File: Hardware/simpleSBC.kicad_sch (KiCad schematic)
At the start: 65 parts, among them J1 Conn_02x07_Odd_Even, J5 USB_A, J6 USB_A, J7 RJ45_Wuerth_7499010121A, J9 Conn_01x06, SW1 SW_Push, U1 STM32MP157FAD1, U2 STMPS2252MTR, U5 USBLC6-4SC6, U6 LAN8742A, X1 ASCO, Y1 32.786, Y2 X53T-C20SSA-25.000MHz

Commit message: First Pass Routing
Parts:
- removed Y2: X53T-C20SSA-25.000MHz, symbol Device:Crystal
- added JP6, JP7: SolderJumper_3_Bridged12, Jumper:SolderJumper-3_P1.3mm_Bridged2Bar12_Pad1.0x1.5mm, symbol Jumper:SolderJumper_3_Bridged12
- added Y3: 24M, SimpleSBC:Crystal_2.00x1.60mm, symbol Device:Crystal_GND24
- JP1, JP2, JP3: footprint (none) -> Resistor_SMD:R_0402_1005Metric; now in the parts list
- SW1: footprint (none) -> Button_Switch_SMD:SW_SPST_Omron_B3FS-101xP
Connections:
- net GND: now also Y3.2, Y3.4
- net IO1: now also U1.1J1 (PA4)
- net IO5: no longer U1.W7 (PF7)
- net IO6: no longer U1.W8 (PG9)
- net PRT1: now also U1.W7 (PF7)
- net PRT2: now also U1.W8 (PG9)
- net USB_~{OC1}: now also U1.V9 (PF9)
- net USB_~{OC2}: now also U1.V7 (PE7)
- net at J5.1 (VBUS): now also JP7.2 (C); no longer U2.6 (OUT2)
- net USB2_D-: now reaches J5.2 (D-), U1.W10 (USB_DM2)
- net USB2_D+: now reaches J5.3 (D+), U1.V10 (USB_DP2)
- net at J6.1 (VBUS): now also JP6.2 (C); no longer U2.7 (OUT1)
- net USB1_D+: now reaches J6.2 (D-), U1.V14 (USB_DP1)
- net USB1_D-: now reaches J6.3 (D+), U1.W14 (USB_DM1)
- net at C44.1, U6.4 (XTAL2): now also Y3.1
- net at C42.1, U6.5 (XTAL1/CLKIN): now also Y3.3
- net +5V renamed VBUS
- new net PMIC_SWOUT: JP6.3 (B)
- new net VBUS1: U2.7 (OUT1)
- new net VBUS2: JP6.1 (A), U2.6 (OUT2)
- no-connect marks 78 -> 75
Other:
- sheet Power ports: added PMIC_SWOUT, PMIC_VBUSOTG; removed none
- note added: "TODO: - ADD PMIC BOOST with disconnect - DAC and ADC pins - Missing Pin Connections - What to do with OTG_VBUS (V16) - Disconnect DSI pins? - Check BOOT pin values - Last checkbox pg. 21 - DRAM LDM Question - OTG VBUS? - RJ45 LEDs?"
- note removed: "TODO: - Missing Pin Connections - What to do with OTG_VBUS (V16) - Disconnect DSI pins? - Check BOOT pin values - Last checkbox pg. 21 - DRAM LDM Question - OTG VBUS? - RJ45 LEDs?"
- moved on the sheet: C42, J5, J9, JP1, R62

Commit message: ERC/DRC Clean
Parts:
- removed J9: Conn_01x06, Connector_PinHeader_2.54mm:PinHeader_1x06_P2.54mm_Vertical, symbol Connector_Generic:Conn_01x06
- added J3, J9: Conn_02x10_Odd_Even, Connector_PinHeader_2.54mm:PinHeader_2x10_P2.54mm_Vertical, symbol Connector_Generic:Conn_02x10_Odd_Even
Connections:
- net +3V3: now also J3.20 (Pin_20), J9.20 (Pin_20)
- net GND: now also J3.19 (Pin_19), J9.19 (Pin_19)
- net PMIC_VBUSOTG: now also JP7.3 (B)
- net VBUS1: now also JP7.1 (A)
- net PD15: now reaches U1.1C2 (PD15)
- net PD15: now also J9.6 (Pin_6)
- net PD1: now reaches U1.A2 (PD1)
- net PD1: now also J9.12 (Pin_12)
- net PC6: now reaches U1.A4 (PC6)
- net PC6: now also J9.13 (Pin_13)
- net PD3: now reaches U1.A7 (PD3)
- net PD3: now also J9.16 (Pin_16)
- net PG15: now reaches U1.B1 (PG15)
- net PG15: now also J9.11 (Pin_11)
- net PE6: now reaches U1.B2 (PE6)
- net PE6: now also J3.16 (Pin_16)
- net PD7: now reaches U1.B3 (PD7)
- net PD7: now also J3.17 (Pin_17)
- net PA15: now reaches U1.B4 (PA15)
- net PA15: now also J9.1 (Pin_1)
- net PG6: now reaches U1.B5 (PG6)
- net PG6: now also J9.18 (Pin_18)
- net PB4: now reaches U1.B6 (PB4)
- net PB4: now also J9.15 (Pin_15)
- net PE5: now reaches U1.B7 (PE5)
- net PE5: now also J9.17 (Pin_17)
- net PA8: now reaches U1.B8 (PA8)
- net PA8: now also J3.15 (Pin_15)
- net PE12: now reaches U1.C1 (PE12)
- net PE12: now also J9.10 (Pin_10)
- net PC7: now reaches U1.C10 (PC7)
- net PC7: now also J9.2 (Pin_2)
- net PE0: now reaches U1.C2 (PE0)
- net PE0: now also J9.9 (Pin_9)
- net PD4: now reaches U1.C3 (PD4)
- net PD4: now also J9.8 (Pin_8)
- net PD5: now reaches U1.C4 (PD5)
- net PD5: now also J3.18 (Pin_18)
- net PD0: now reaches U1.C5 (PD0)
- net PD0: now also J9.14 (Pin_14)
- net PA9: now reaches U1.C6 (PA9)
- net PA9: now also J3.2 (Pin_2)
- net PB15: now reaches U1.C8 (PB15)
- net PB15: now also J3.14 (Pin_14)
- net PB9: now reaches U1.C9 (PB9)
- net PB9: now also J3.1 (Pin_1)
- net PG12: now reaches U1.D1 (PG12)
- net PG12: now also J3.13 (Pin_13)
- net PE15: now reaches U1.D3 (PE15)
- net PE15: now also J9.7 (Pin_7)
- net PD8: now reaches U1.E1 (PD8)
- net PD8: now also J3.12 (Pin_12)
- net PE13: now reaches U1.E3 (PE13)
- net PE13: now also J3.11 (Pin_11)
- net PE2: now reaches U1.P1 (PE2)
- net PE2: now also J9.3 (Pin_3)
- net PC2: now reaches U1.P2 (PC2)
- net PC2: now also J9.4 (Pin_4)
- net PB1: now reaches U1.U1 (PB1)
- net PB1: now also J3.7 (Pin_7)
- net PB0: now reaches U1.U2 (PB0)
- net PB0: now also J3.10 (Pin_10)
- net PC0: now reaches U1.U4 (PC0)
- net PC0: now also J3.4 (Pin_4)
- net PG10: now reaches U1.U7 (PG10)
- net PG10: now also J9.5 (Pin_5)
- net PD11: now reaches U1.U8 (PD11)
- net PD11: now also J3.3 (Pin_3)
- net PB12: now reaches U1.V3 (PB12)
- net PB12: now also J3.9 (Pin_9)
- net PB8: now reaches U1.V4 (PB8)
- net PB8: now also J3.8 (Pin_8)
- net IO1: no longer names the net of U1.1J1 (PA4)
- net IO3 renamed PA6
- net PA6: now also J3.6 (Pin_6)
- net IO4 renamed PF11
- net PF11: now also J3.5 (Pin_5)
- no-connect marks 75 -> 42
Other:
- moved on the sheet: JP7, R60

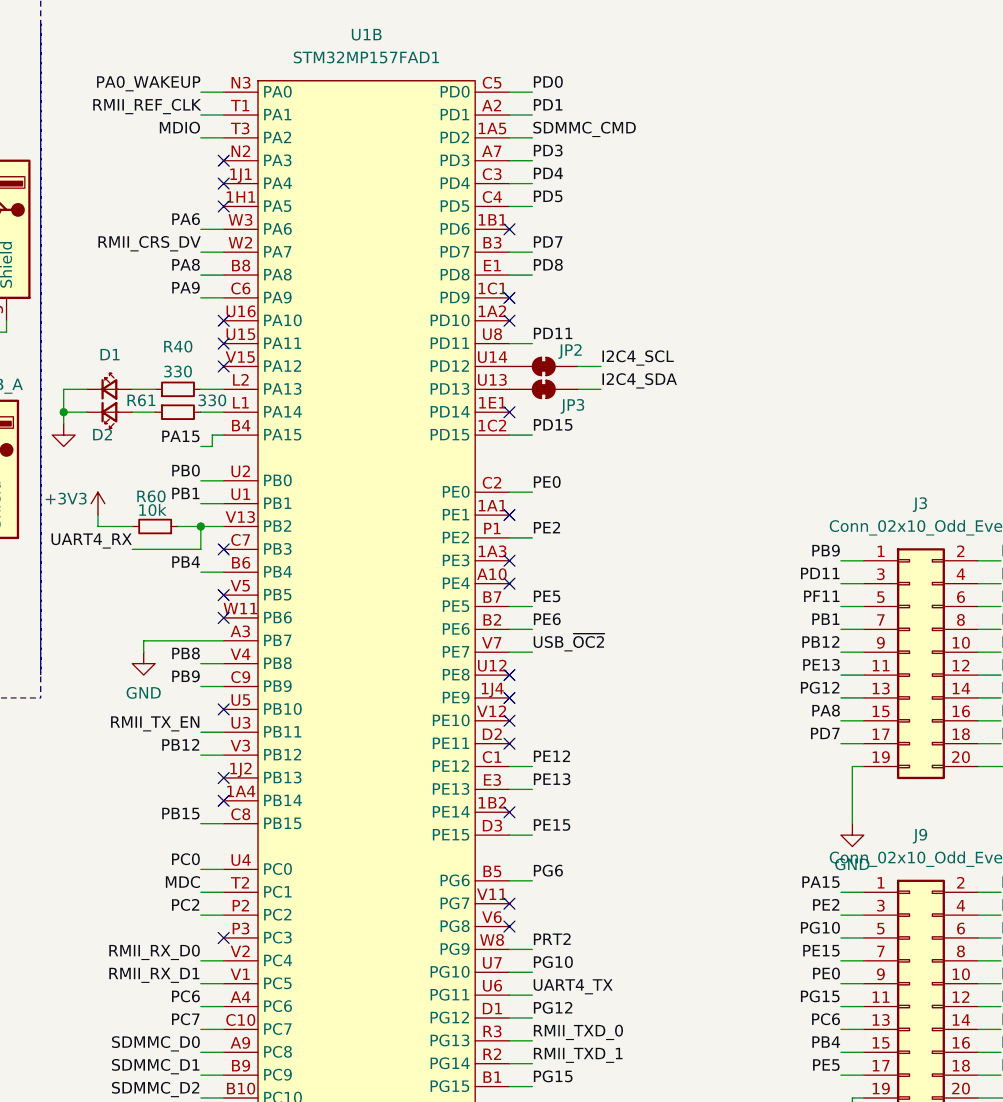
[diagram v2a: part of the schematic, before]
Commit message: Redo DRAM Length Tuning
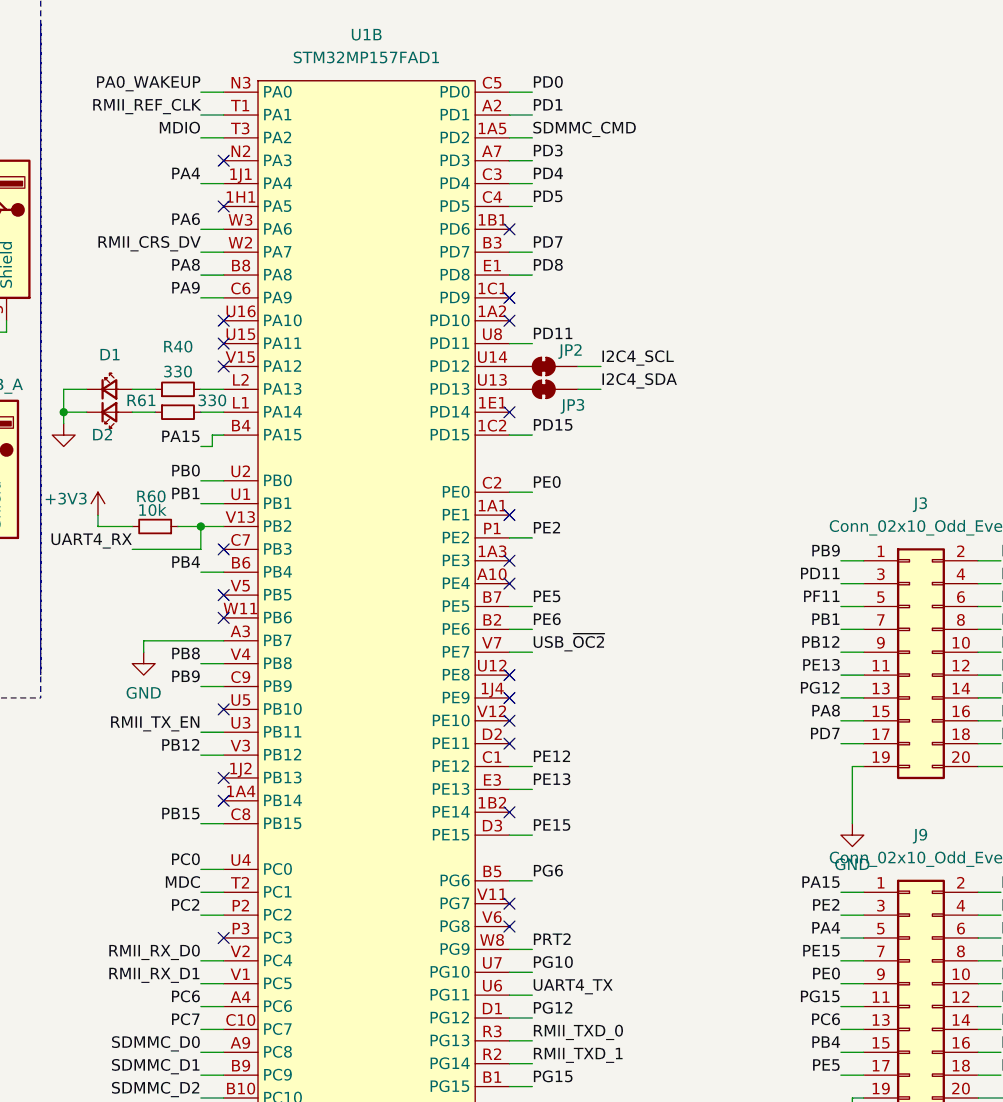
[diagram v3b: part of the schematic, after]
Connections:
- net PG10: no longer J9.5 (Pin_5)
- net PA4: now reaches U1.1J1 (PA4)
- net PA4: now also J9.5 (Pin_5)
- no-connect marks 42 -> 41
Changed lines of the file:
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@@
 	)
 	(no_connect
-		(at 213.36 34.29)
-	)
-	(no_connect
 		(at 245.11 46.99)
 	)
@@
 	(wire
 		(pts
+			(xy 210.82 34.29) (xy 213.36 34.29)
+		)
+		(stroke
+			(width 0)
+			(type default)
+		)
+	)
+	(wire
+		(pts
 			(xy 107.95 158.75) (xy 110.49 158.75)
 		)
@@
 		)
 	)
-	(label "PG10"
+	(label "PA4"
 		(at 281.94 118.11 180)
 		(effects
@@
 		(effects
 			(font
+				(size 1.27 1.27)
+			)
+			(justify right bottom)
+		)
+	)
+	(label "PA4"
+		(at 210.82 34.29 180)
+		(effects
+			(font

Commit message: Reconnect Nets after length tuning
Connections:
- net PG10: no longer names the net of U1.U7 (PG10)
- no-connect marks 41 -> 42
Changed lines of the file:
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@@
 	)
 	(no_connect
+		(at 245.11 121.92)
+	)
+	(no_connect
 		(at 29.21 182.88)
 	)
@@
 	(wire
 		(pts
-			(xy 245.11 121.92) (xy 247.65 121.92)
-		)
-		(stroke
-			(width 0)
-			(type default)
-		)
-	)
-	(wire
-		(pts
 			(xy 186.69 49.53) (xy 186.69 50.8)
 		)
@@
 		)
 	)
-	(label "PG10"
-		(at 247.65 121.92 0)
-		(effects
-			(font
-				(size 1.27 1.27)
-			)
-			(justify left bottom)
-		)
-	)

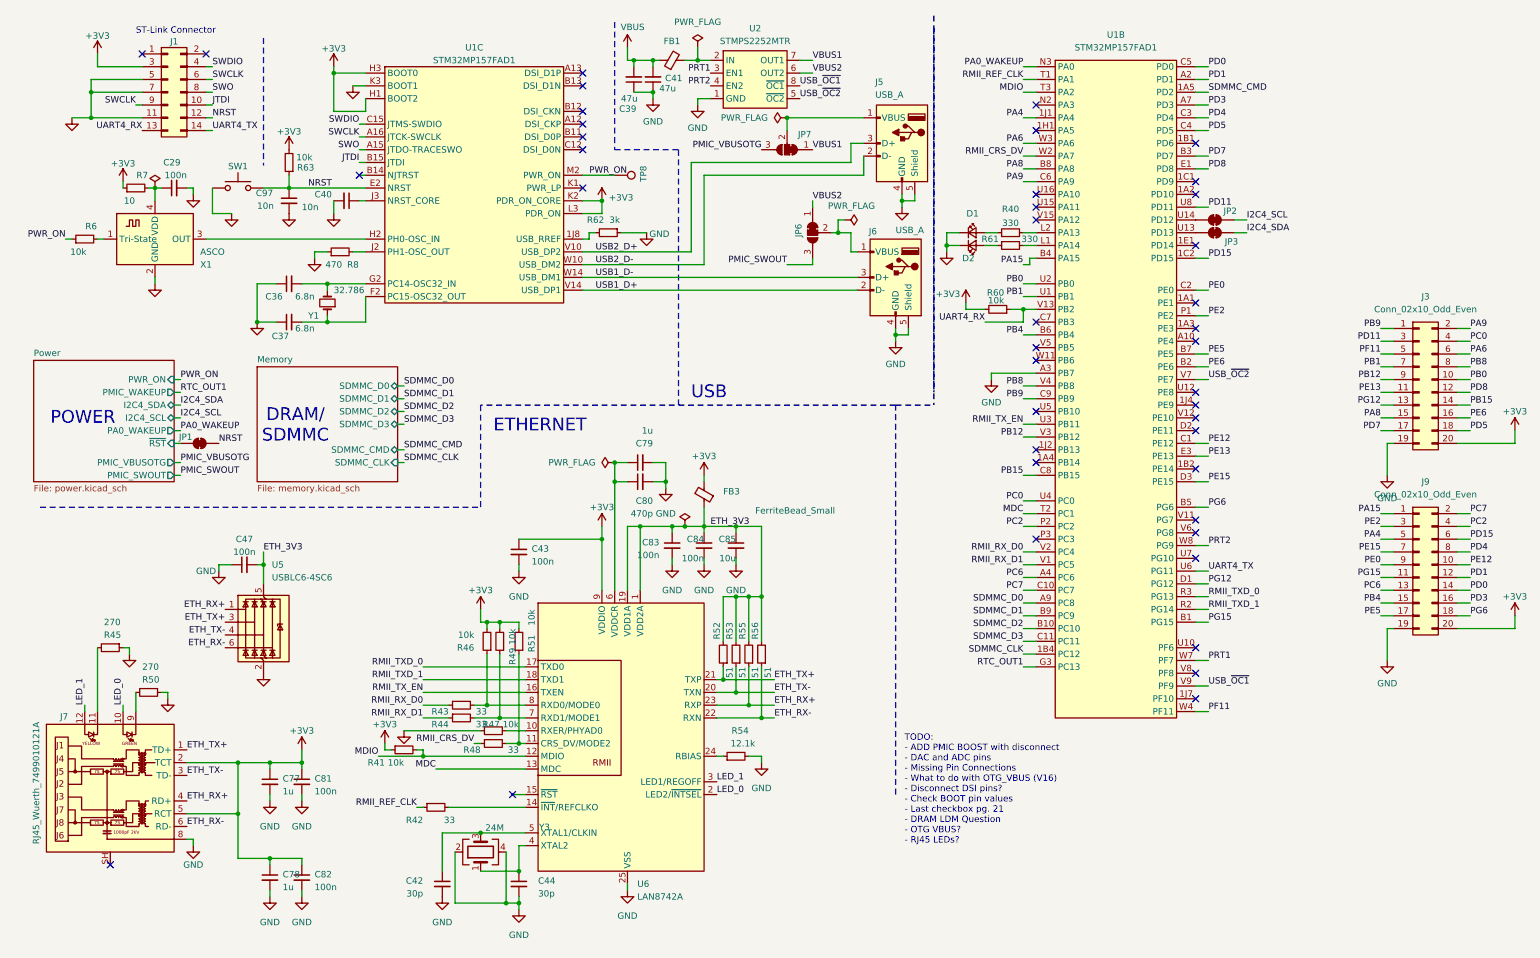
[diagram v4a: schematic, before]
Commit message: Add Boot selection jumpers
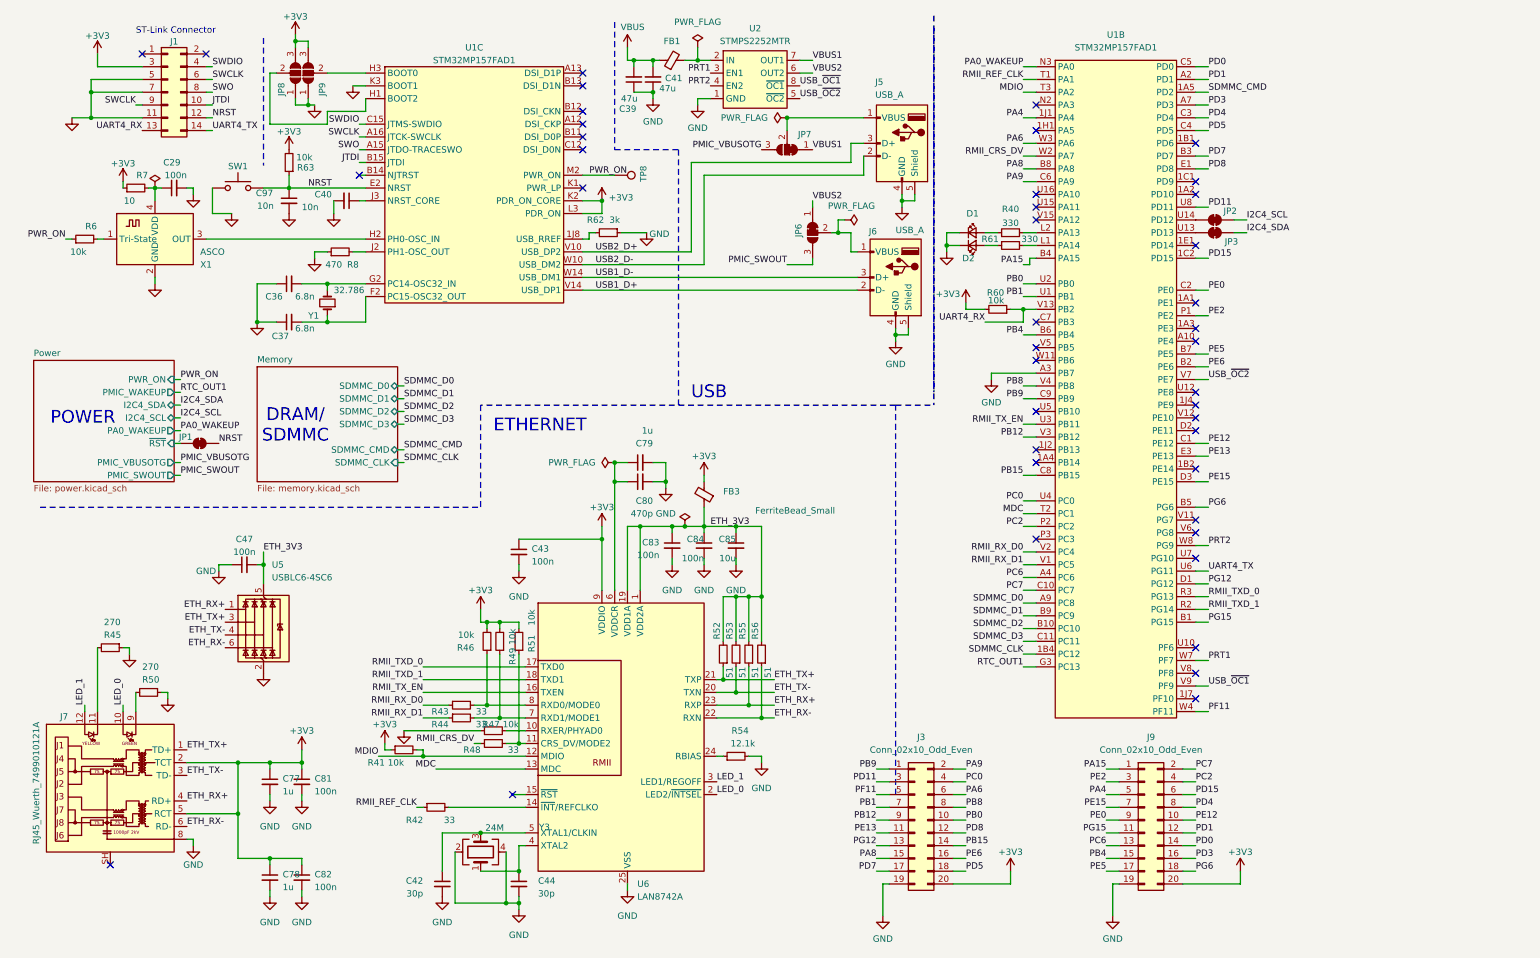
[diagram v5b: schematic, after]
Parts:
- added JP8, JP9: SolderJumper_3_Open, Jumper:SolderJumper-3_P1.3mm_Open_Pad1.0x1.5mm, symbol Jumper:SolderJumper_3_Open
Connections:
- net +3V3: now also JP8.3 (B), JP9.3 (B); no longer U1.H1 (BOOT2), U1.H3 (BOOT0)
- net GND: now also JP8.1 (A), JP9.1 (A)
- new net: JP9.2 (C), U1.H3 (BOOT0)
- new net: JP8.2 (C), U1.H1 (BOOT2)
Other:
- note removed: "TODO: - ADD PMIC BOOST with disconnect - DAC and ADC pins - Missing Pin Connections - What to do with OTG_VBUS (V16) - Disconnect DSI pins? - Check BOOT pin values - Last checkbox pg. 21 - DRAM LDM Question - OTG VBUS? - RJ45 LEDs?"
- moved on the sheet: J3, J9

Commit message: Add USB enable pulldowns
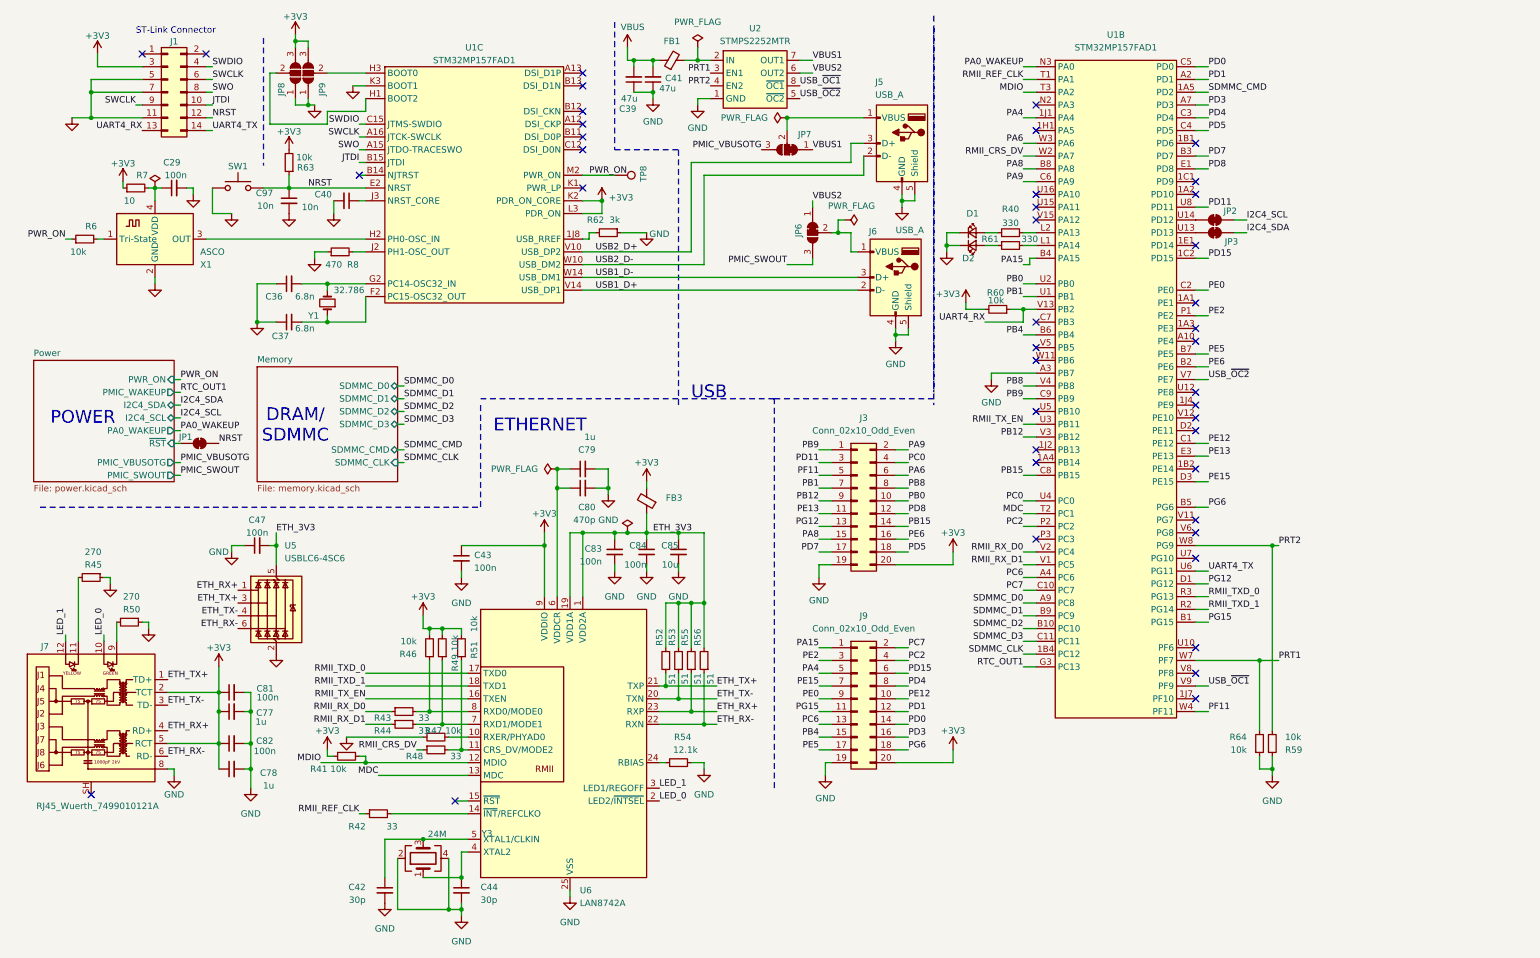
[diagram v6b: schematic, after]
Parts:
- added R59, R64: 10k, Resistor_SMD:R_0402_1005Metric, symbol Device:R_Small
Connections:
- net GND: now also R59.1, R64.1
- net PRT1: now also R64.2
- net PRT2: now also R59.2
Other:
- moved on the sheet: C42, C43, C44, C47, C77, C78, C79, C80, C81, C82, C83, C84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

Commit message: prepare for assembly
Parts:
- C29, C43, C47, C81, C82, C83, C84: JLCPCB Part # (none) -> C1525
- C36, C37: value 6.8n -> 10p; JLCPCB Part # (none) -> C32949
- C39, C41: value 47u -> 100n; JLCPCB Part # (none) -> C1525
- C40, C97: JLCPCB Part # (none) -> C15195
- C42, C44: value 30p -> 10p; JLCPCB Part # (none) -> C32949
- C77, C78, C79: JLCPCB Part # (none) -> C52923
- C80: value 470p -> 220p; JLCPCB Part # (none) -> C1530
- C85: JLCPCB Part # (none) -> C15850
- D1: JLCPCB Part # (none) -> C2296
- D2: JLCPCB Part # (none) -> C2297
- FB1, FB3: JLCPCB Part # (none) -> C1002
- J1, J3, J5, J6, J7, J9, JP1, JP2, JP3, JP6, JP7, JP8, JP9, SW1, TP8: now not fitted
- R40, R61: JLCPCB Part # (none) -> C25104
- R41, R46, R47, R49, R51, R59, R6, R60, R63, R64: JLCPCB Part # (none) -> C25744
- R42, R43, R44, R48: JLCPCB Part # (none) -> C25105
- R45, R50: value 270 -> 330; JLCPCB Part # (none) -> C25104
- R52, R53, R55, R56: value 51 -> 56; JLCPCB Part # (none) -> C25127
- R54: JLCPCB Part # (none) -> C25863
- R62: JLCPCB Part # (none) -> C881171
- R7: JLCPCB Part # (none) -> C25077
- R8: JLCPCB Part # (none) -> C25117
- U1: JLCPCB Part # (none) -> C1236719
- U2: JLCPCB Part # (none) -> C2680426; now not fitted
- U5: JLCPCB Part # (none) -> C111212
- U6: JLCPCB Part # (none) -> C220794
- X1: JLCPCB Part # (none) -> C19078199
- Y1: JLCPCB Part # (none) -> C5341287
- Y3: JLCPCB Part # (none) -> C127895
